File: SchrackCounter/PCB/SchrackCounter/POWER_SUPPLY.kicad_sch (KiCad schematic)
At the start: 7 parts, among them J1 Conn_01x02_Pin, U1 LM1084-3.3

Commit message: PCB layout update
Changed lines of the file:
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@@
 		(dnp no)
 		(property "Reference" "C4"
-			(at 179.07 64.77 0)
+			(at 178.435 61.595 0)
 			(effects
 				(font
@@
 		)
 		(property "Value" "10uF.stabl"
-			(at 179.07 67.31 0)
+			(at 178.435 63.5 0)
 			(effects
 				(font
@@
 		(dnp no)
 		(property "Reference" "C2"
-			(at 123.825 119.38 0)
+			(at 123.825 120.015 0)
 			(effects
 				(font
@@
 		(on_board yes)
 		(dnp no)
-		(fields_autoplaced yes)
 		(property "Reference" "#PWR03"
 			(at 158.75 78.74 0)
@@
 		)
 		(property "Value" "GND"
-			(at 158.75 77.47 0)
+			(at 158.75 76.2 0)
 			(effects
 				(font
@@
 		(dnp no)
 		(property "Reference" "C3"
-			(at 135.89 64.77 0)
+			(at 137.795 62.23 0)
 			(effects
 				(font
@@
 		)
 		(property "Value" "10uF.stabl"
-			(at 129.54 67.31 0)
+			(at 132.08 64.135 0)
 			(effects
 				(font
@@
 		(dnp no)
 		(property "Reference" "C1"
-			(at 113.665 119.38 0)
-			(effects
-				(font
+			(at 113.665 120.015 0)
+			(effects
+				(font

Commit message: SchrackCounter
PCB Finished
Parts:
- C1: renamed from C3; value 10uF.stabl -> 10uF
- C4: value 10uF.stabl -> 10uF
- renumbered C1 to C2, C2 to C3
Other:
- moved on the sheet: C1, C4, J1, U1

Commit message: PCB update
pcb redesign
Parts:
- removed J1: Conn_01x02_Pin, Connector_JST:JST_XH_B2B-XH-A_1x02_P2.50mm_Vertical, symbol Connector:Conn_01x02_Pin
- added SW1: SW_SPST, Connector_JST:JST_XH_B2B-XH-A_1x02_P2.50mm_Vertical, symbol Switch:SW_SPST
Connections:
- net +5V: now also SW1.1 (A)
- net VBATT: now also SW1.2 (B)
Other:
- moved on the sheet: BT1, C1, C2, C3, C4, U1

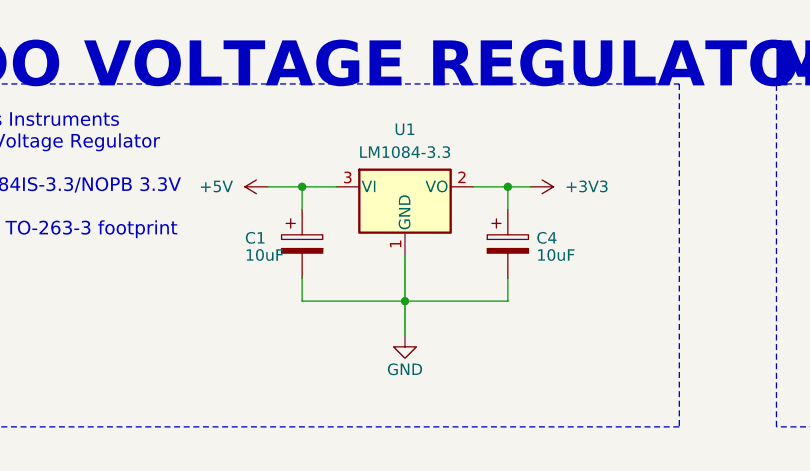
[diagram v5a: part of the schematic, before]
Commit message: SchrackMulticlock and Counter update
Schematic update for both
PCB update for Counter
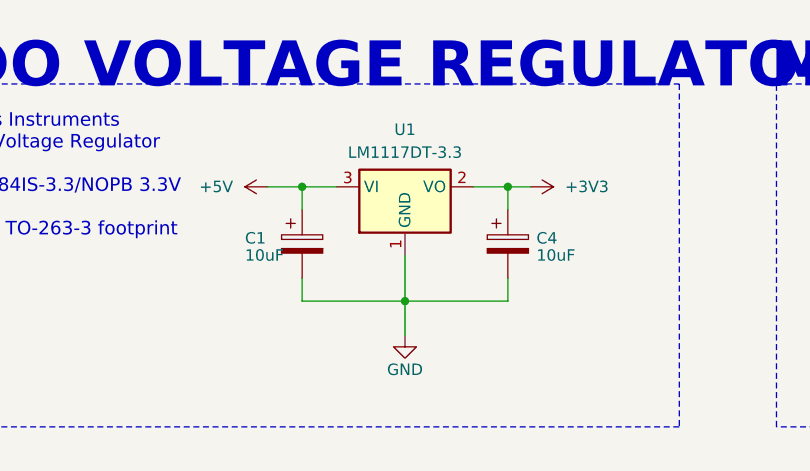
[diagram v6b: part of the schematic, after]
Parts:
- removed U1: LM1084-3.3, Package_TO_SOT_SMD:TO-263-3_TabPin2, symbol Regulator_Linear:LM1084-3.3
- added U1: LM1117DT-3.3, Package_TO_SOT_SMD:TO-252-3_TabPin2, symbol Regulator_Linear:LM1117DT-3.3
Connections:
- net +3V3: now also U1.2 (VO)
- net +5V: now also U1.3 (VI)
- net GND: now also U1.1 (GND)
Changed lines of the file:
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@@
+	)
+	(symbol
+		(lib_id "Regulator_Linear:LM1117DT-3.3")
+		(at 113.03 59.69 0)
+		(unit 1)
+		(exclude_from_sim no)
+		(in_bom yes)
+		(on_board yes)
+		(dnp no)
+		(fields_autoplaced yes)
+		(property "Reference" "U1"
+			(at 113.03 53.34 0)
+			(effects
+				(font
+					(size 1.27 1.27)
+				)
+			)
+		)
+		(property "Value" "LM1117DT-3.3"
+			(at 113.03 55.88 0)
+			(effects
+				(font
+					(size 1.27 1.27)
+				)
+			)
+		)
+		(property "Footprint" "Package_TO_SOT_SMD:TO-252-3_TabPin2"
+			(at 113.03 59.69 0)
+			(effects
+				(font
+					(size 1.27 1.27)
+				)
+				(hide yes)
+			)
+		)
+		(property "Datasheet" "http://www.ti.com/lit/ds/symlink/lm1117.pdf"
+			(at 113.03 59.69 0)
+			(effects
+				(font
+					(size 1.27 1.27)
+				)
+				(hide yes)
+			)
+		)
+		(property "Description" "800mA Low-Dropout Linear Regulator, 3.3V fixed output, TO-252"
+			(at 113.03 59.69 0)
+			(effects
+				(font
+					(size 1.27 1.27)
+				)
+				(hide yes)
+			)
+		)
+		(pin "1"
+		)
+		(pin "2"
+		)
+		(pin "3"
+		)
+		(instances
+			(project ""
+				(path "/d96f2ffc-3f4c-4f71-b693-29f6b8c3245d/2b0bd697-1473-4a31-8990-1278f12dea07"
+					(reference "U1")
+					(unit 1)
+				)
+			)
+		)
 	)
 	(symbol
@@
 					(unit 1)
 				)
-			)
-		)
-	)
-	(symbol
-		(lib_id "Regulator_Linear:LM1084-3.3")
-		(at 113.03 59.69 0)
-		(unit 1)
-		(exclude_from_sim no)
-		(in_bom yes)
-		(on_board yes)
-		(dnp no)
-		(fields_autoplaced yes)
-		(property "Reference" "U1"
-			(at 113.03 53.34 0)
-			(effects
-				(font
-					(face "Bahnschrift")
-					(size 1.27 1.27)
-				)
-			)
-		)
-		(property "Value" "LM1084-3.3"
-			(at 113.03 55.88 0)
-			(effects
-				(font
-					(face "Bahnschrift")
-					(size 1.27 1.27)
-				)
-			)
-		)
-		(property "Footprint" "Package_TO_SOT_SMD:TO-263-3_TabPin2"
-			(at 113.03 53.34 0)
-			(effects
-				(font
-					(face "Bahnschrift")
-					(size 1.27 1.27)
-					(italic yes)
-				)
-				(hide yes)
-			)
-		)
-		(property "Datasheet" "http://www.ti.com/lit/ds/symlink/lm1084.pdf"
-			(at 113.03 59.69 0)
-			(effects
-				(font
-					(face "Bahnschrift")
-					(size 1.27 1.27)
-				)
-				(hide yes)
-			)
-		)
-		(property "Description" ""
-			(at 113.03 59.69 0)
-			(effects
-				(font
-					(size 1.27 1.27)
-				)
-				(hide yes)
-			)
-		)
-		(pin "1"
-		)
-		(pin "2"
-		)
-		(pin "3"
-		)
-		(instances
-			(project "SchrackCounter"
-				(path "/d96f2ffc-3f4c-4f71-b693-29f6b8c3245d/2b0bd697-1473-4a31-8990-1278f12dea07"
-					(reference "U1")
-					(unit 1)
-				)

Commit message: mouser link
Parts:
- U1: mouser (none) -> https://cz.mouser.com/ProductDetail/Texas-Instruments/LM111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
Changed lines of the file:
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@@
+			)
+		)
+		(property "mouser" "https://cz.mouser.com/ProductDetail/Texas-Instruments/LM1117DT-3.3-NOPB?qs=X1J7HmVL2ZHOT670myqy2w%3D%3D"
+			(at 113.03 59.69 0)
+			(effects
+				(font
+					(size 1.27 1.27)
+				)
+				(hide yes)
 			)
 		)

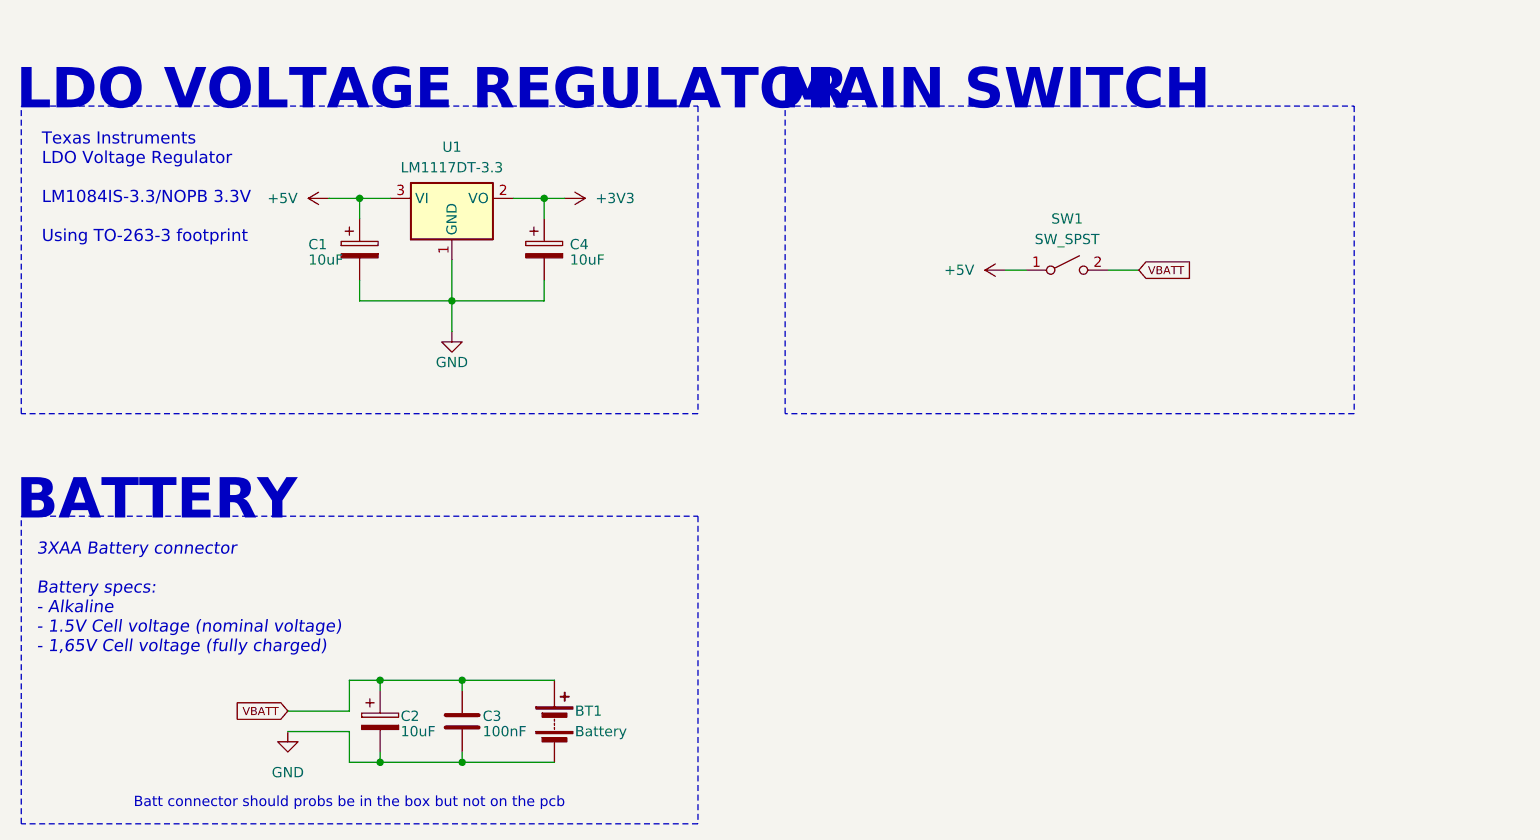
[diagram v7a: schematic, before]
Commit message: SchrackMulticlock and Counter pcb updates
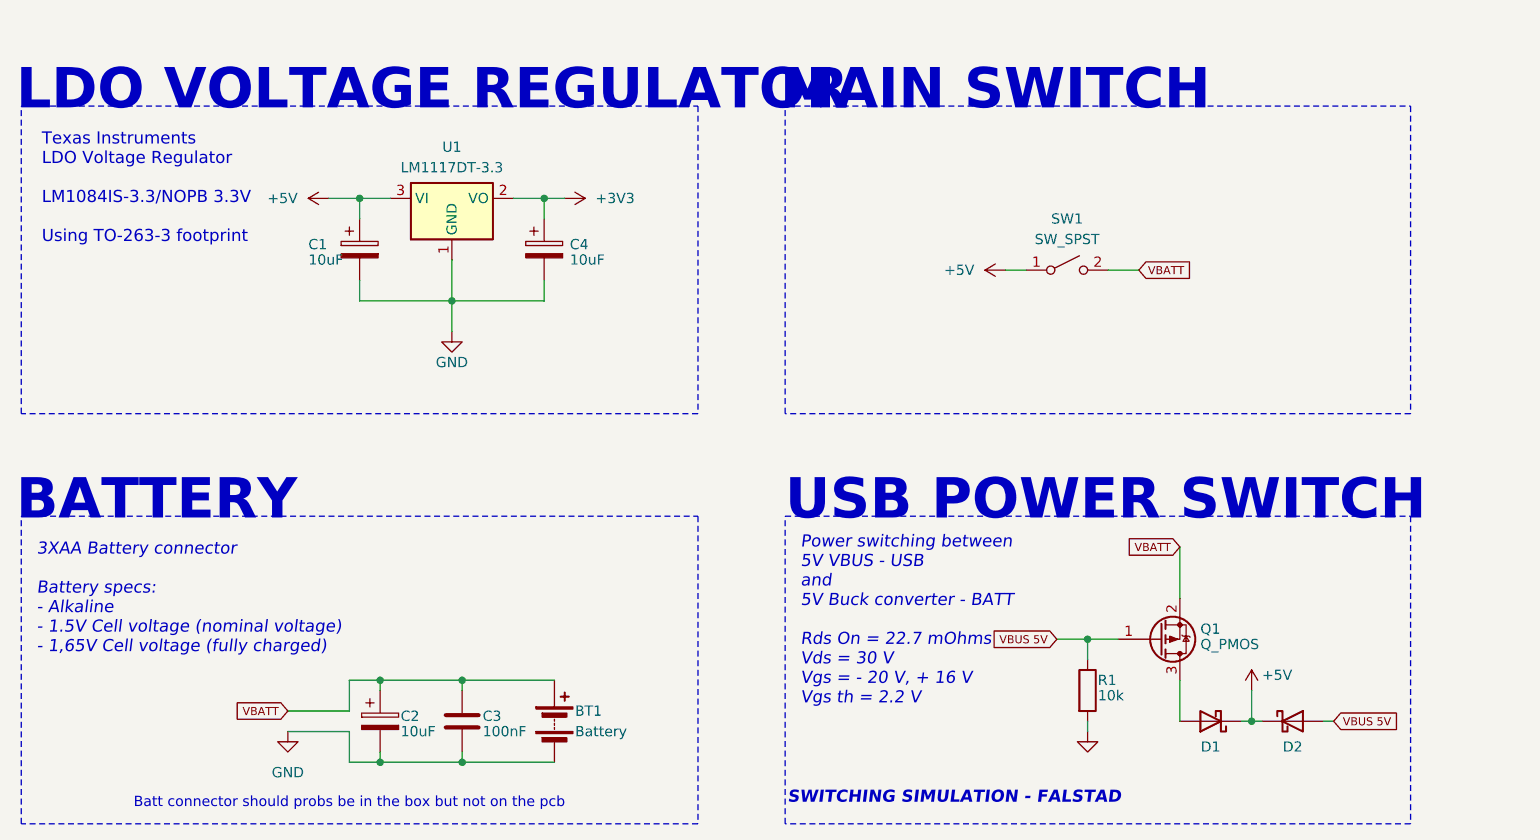
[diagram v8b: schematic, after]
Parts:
- added D1, D2: D_Schottky, Diode_SMD:D_1206_3216Metric_Pad1.42x1.75mm_HandSolder, symbol Device:D_Schottky
- added Q1: Q_PMOS, Package_TO_SOT_SMD:SOT-23-3, symbol Device:Q_PMOS_GSD
- added R1: 10k, Resistor_SMD:R_0805_2012Metric_Pad1.20x1.40mm_HandSolder, symbol Device:R
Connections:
- net +5V: now also D1.1 (K), D2.1 (K)
- net GND: now also R1.2
- net VBATT: now also Q1.2 (S)
- new net: D1.2 (A), Q1.3 (D)
- new net VBUS 5V: D2.2 (A), Q1.1 (G), R1.1
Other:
- note added: "Power switching between 5V VBUS - USB and 5V Buck converter - BATT"
- note added: "Rds On = 22.7 mOhms Vds = 30 V Vgs = - 20 V, + 16 V Vgs th = 2.2 V"
- note added: "SWITCHING SIMULATION - FALSTAD"
- note added: "USB POWER SWITCH"
